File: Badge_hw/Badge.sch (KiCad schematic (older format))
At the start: 2 parts

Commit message: + Power Supply in process (OLinuXino redrawing)
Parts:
- added C? (x6): 10uF, symbol C
- added C? (x3): 1uF, symbol C
- added C?: 1nF, symbol C
- added D?: CHGLED, symbol LED
- added L?: 2.2uH, Inductors:IND_0402, symbol L
- added R1: 240, symbol R
- added R? (x2): 1, symbol R
- added R? (x5): 2.2k, symbol R
- added R?: 200k, symbol R
- added R?: 0.03, symbol R
- added SW?: RESET, symbol SW_PUSH_SMALL_H
- added SW?: PWR_BUT, symbol SW_PUSH_SMALL_H
- gave numbers to parts that had none: 2
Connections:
- net labels added: +BATT, GND
- wire segments 0 -> 67
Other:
- moved on the sheet: DD2

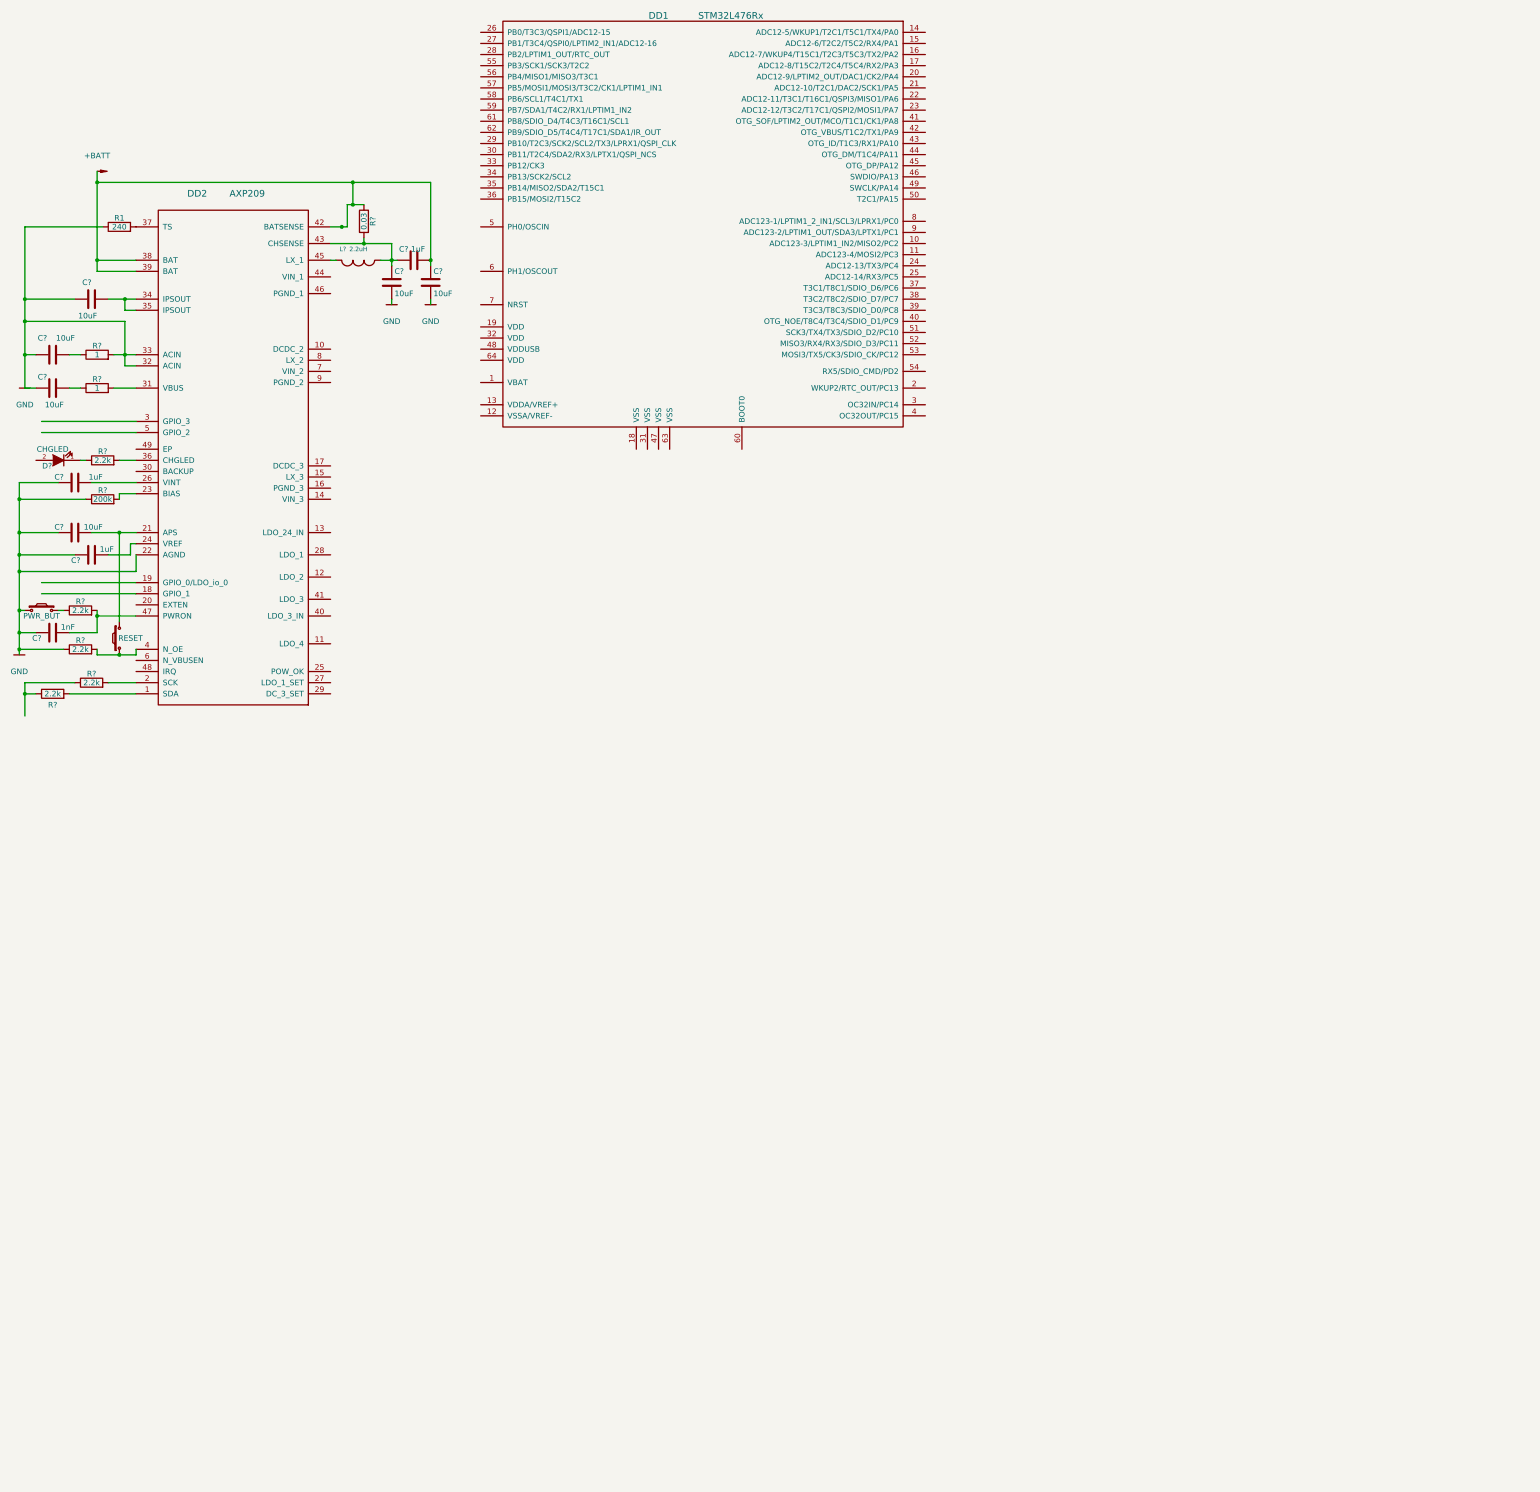
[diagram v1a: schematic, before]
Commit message: * added display component & interface
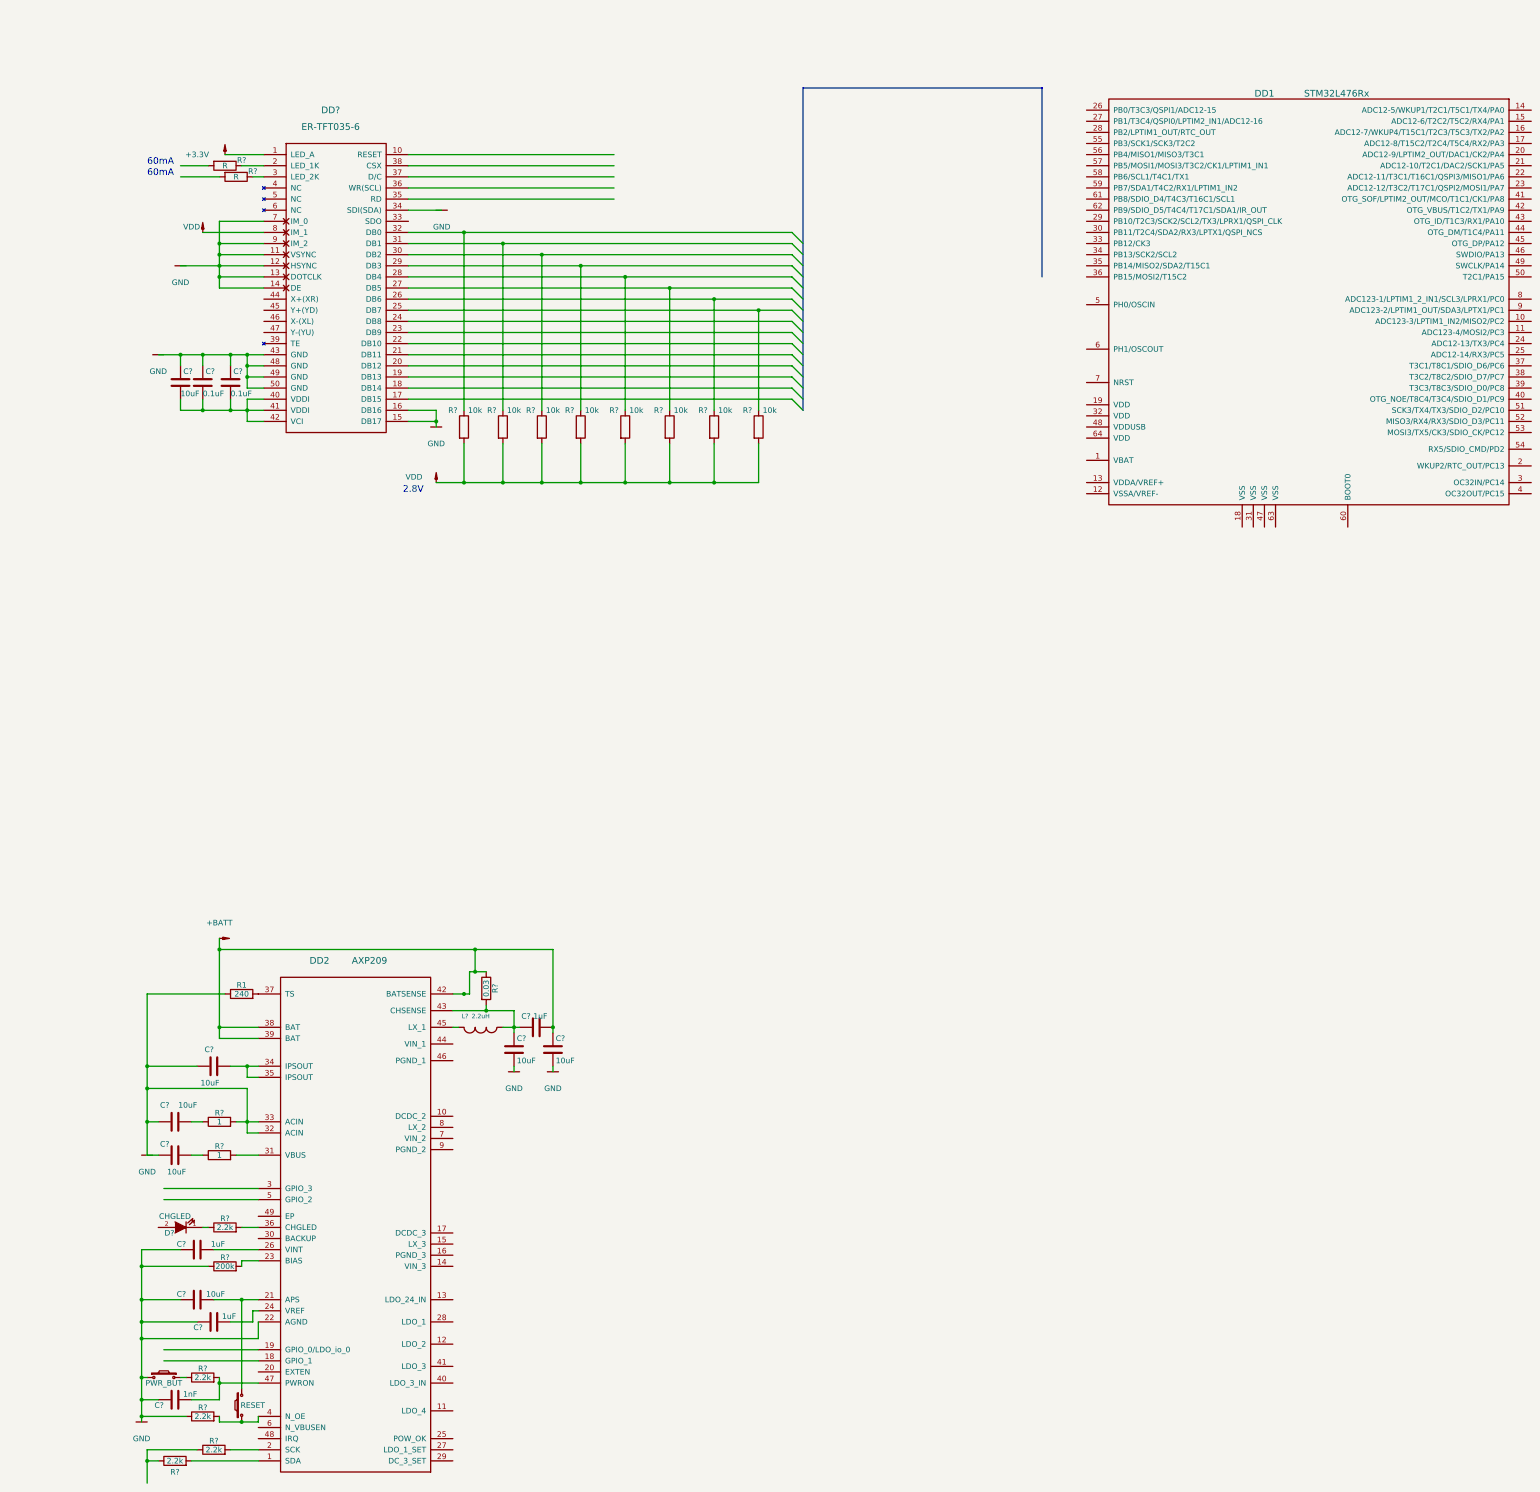
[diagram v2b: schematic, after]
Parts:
- added C? (x2): 0.1uF, symbol C
- added C?: 10uF, symbol C
- added DD?: ER-TFT035-6, symbol ER-TFT035-6
- added R? (x2): R, symbol R
- added R? (x8): 10k, symbol R
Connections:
- net labels added: +3.3V, VDD
- wire segments 67 -> 137
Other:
- note added: "2.8V"
- note added: "60mA"
- moved on the sheet: C?, D?, DD1, DD2, L?, R1, R?

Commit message: + Touch Interface
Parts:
- added C?: 10u, symbol C
- added C? (x2): 0.1u, symbol C
- added C?: 1u, symbol C
- added DD?: STMPE811, QFN_DFN:QFN16_4x4_H, symbol STMPE811
- added L?: BLM15AG102, Inductors:IND_0402, symbol L
- added R?: 10k, symbol R
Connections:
- net labels added: 2.8V, 60mA, LED_CS, LED_D/I_SLC, LED_RESET, LED_RX, LED_TX, LED_X+, LED_X-, LED_Y+, LED_Y-, SCL, SDA, TOUCH_INT, TOUCH_PWR
- wire segments 137 -> 261
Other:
- note added: "LED"
- note added: "MCU"
- note added: "POWER"
- note added: "TOUCH"
- note removed: "2.8V"
- note removed: "60mA"
- moved on the sheet: C?, D?, DD2, L?, R1, R?

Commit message: AXP209_full_power_supply_circuit
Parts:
- added C? (x11): 22uF, symbol C
- added C?: 100nF, symbol C
- added C?: 47pF, symbol C
- added C?: 470uF, symbol CP
- added C?: 22pF, symbol C
- added C?: 10nF, symbol C
- added C?: 3.3nF, symbol C
- added C? (x2): NA, symbol CP
- added C? (x10): 10uF, symbol C
- added C? (x2): 1nF, symbol C
- added CON?: BARREL_JACK, symbol BARREL_JACK
- added D? (x2): SY8008C, symbol SY8008C
- added D?: MP1482DS, symbol MP1482DS
- added D?: SY7208, symbol SY7208
- added D? (x2): D_Shottky, symbol D_Shottky
- added D?: D, symbol D
- added D?: LED, symbol LED
- added L? (x6): 2.2uH, Inductors:IND_0402, symbol L
- added LIPO_BAT?: DW02R, symbol DW02R
- added Q?: MOSFET_P_3LEAD, symbol MOSFET_P_3LEAD
- added R?: 1.1k, symbol R
- added R?: 8.2k, symbol R
- added R?: 100k, symbol R
- added R?: 22k, symbol R
- added R? (x2): 4.99k, symbol R
- added R?: 3.3k, symbol R
- added R?: 47k, symbol R
- added R? (x2): 2.2k, symbol R
- added R?: 1.05k, symbol R
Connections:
- net labels added: +1.5V, +3.0VA, +5V, 1.2V_CPU, 1.2V_INT, 5VEXT, 6-16VDC, ?, EXTEN, IPSOUT, RESET_N, TVS?, VINT
- wire segments 261 -> 366
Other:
- moved on the sheet: C?, D?, DD2, L?, R1, R?
